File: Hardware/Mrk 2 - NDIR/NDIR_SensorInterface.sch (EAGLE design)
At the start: 6 parts, among them J1 CONN_I2C_SENSOR_BOARD_MOUNT_T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, J2 CONN_42.54, Q1 DMG3404

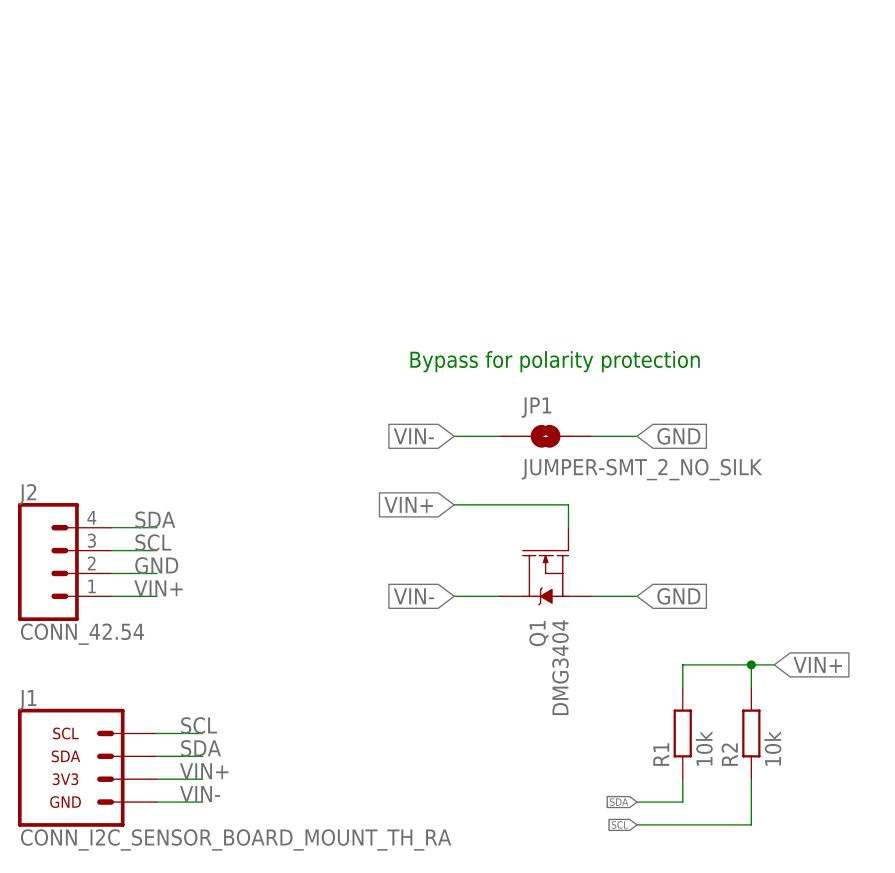
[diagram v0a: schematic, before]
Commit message: Fixed production version naming of Mrk 2 design
Added layout dimensions
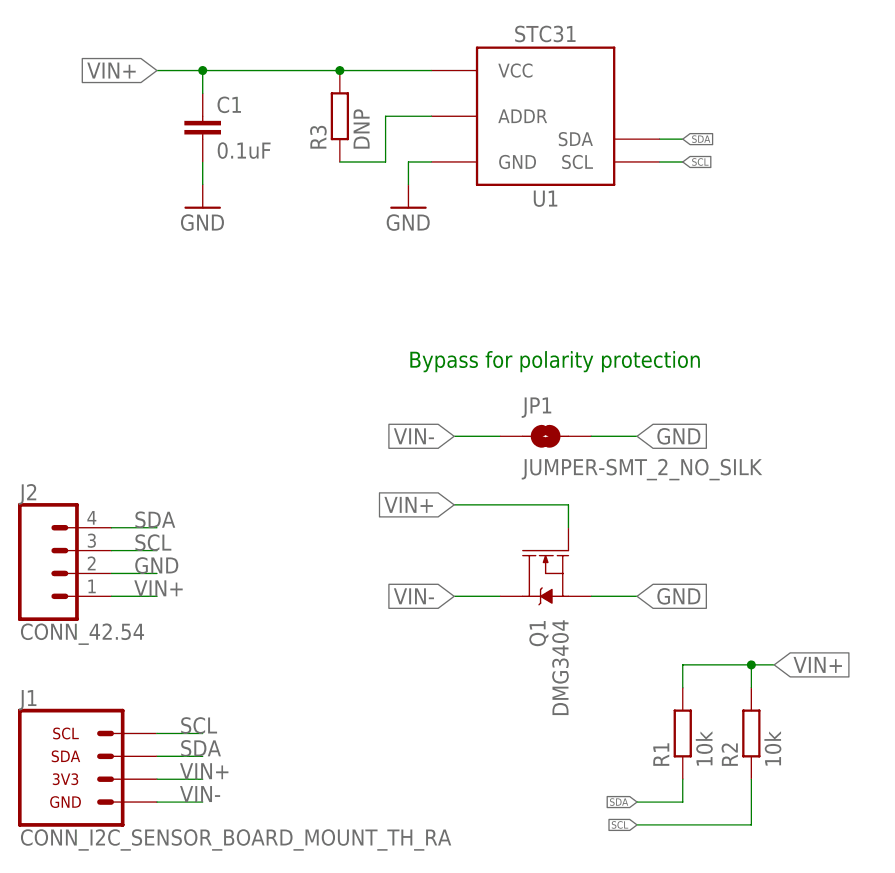
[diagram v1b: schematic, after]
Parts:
- added C1: 0.1uF, bschulz_passives:C-EU0.1UFC0603
- added R3: DNP, bschulz_passives:R-EU_R0603
- added U1: STC31, bschulz:STC31
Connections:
- new net N$2: R3.1, U1.ADDR
- net GND: now also C1.2, U1.GND
- net SCL: now also U1.SCL
- net SDA: now also U1.SDA
- net VIN+: now also C1.1, R3.2, U1.VCC
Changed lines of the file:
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@@
 <layer number="56" name="wert" color="7" fill="1" visible="no" active="no"/>
 <layer number="57" name="tCAD" color="7" fill="1" visible="no" active="no"/>
+<layer number="58" name="bCAD" color="7" fill="1" visible="no" active="no"/>
 <layer number="59" name="tCarbon" color="7" fill="1" visible="no" active="no"/>
 <layer number="60" name="bCarbon" color="7" fill="1" visible="no" active="no"/>
@@
 <layer number="128" name="_bValues" color="7" fill="1" visible="no" active="yes"/>
 <layer number="129" name="Mask" color="7" fill="1" visible="no" active="yes"/>
+<layer number="130" name="SMDSTROOK" color="7" fill="1" visible="no" active="no"/>
 <layer number="131" name="tAdjust" color="7" fill="1" visible="no" active="yes"/>
 <layer number="132" name="bAdjust" color="7" fill="1" visible="no" active="yes"/>
+<layer number="133" name="bottom_silk" color="7" fill="1" visible="no" active="no"/>
+<layer number="134" name="mbFinish" color="7" fill="1" visible="no" active="no"/>
+<layer number="135" name="mtGlue" color="7" fill="1" visible="no" active="no"/>
+<layer number="136" name="mbGlue" color="7" fill="1" visible="no" active="no"/>
+<layer number="137" name="mtTest" color="7" fill="1" visible="no" active="no"/>
+<layer number="138" name="mbTest" color="7" fill="1" visible="no" active="no"/>
+<layer number="139" name="mtKeepout" color="7" fill="1" visible="no" active="no"/>
+<layer number="140" name="mbKeepout" color="7" fill="1" visible="no" active="no"/>
+<layer number="141" name="mtRestrict" color="7" fill="1" visible="no" active="no"/>
+<layer number="142" name="mbRestrict" color="7" fill="1" visible="no" active="no"/>
+<layer number="143" name="mvRestrict" color="7" fill="1" visible="no" active="no"/>
 <layer number="144" name="Drill_legend" color="7" fill="1" visible="no" active="yes"/>
+<layer number="145" name="mHoles" color="7" fill="1" visible="no" active="no"/>
+<layer number="146" name="mMilling" color="7" fill="1" visible="no" active="no"/>
+<layer number="147" name="mMeasures" color="7" fill="1" visible="no" active="no"/>
+<layer number="148" name="mDocument" color="7" fill="1" visible="no" active="no"/>
+<layer number="149" name="mReference" color="7" fill="1" visible="no" active="no"/>
 <layer number="150" name="Notes" color="7" fill="1" visible="no" active="yes"/>
 <layer number="151" name="HeatSink" color="7" fill="1" visible="no" active="yes"/>
@@
 <layer number="154" name="FabDoc2" color="7" fill="1" visible="no" active="yes"/>
 <layer number="155" name="FabDoc3" color="7" fill="1" visible="no" active="yes"/>
+<layer number="166" name="AntennaArea" color="7" fill="1" visible="no" active="no"/>
+<layer number="168" name="4mmHeightArea" color="7" fill="1" visible="no" active="no"/>
+<layer number="191" name="mNets" color="7" fill="1" visible="no" active="no"/>
+<layer number="192" name="mBusses" color="7" fill="1" visible="no" active="no"/>
+<layer number="193" name="mPins" color="7" fill="1" visible="no" active="no"/>
+<layer number="194" name="mSymbols" color="7" fill="1" visible="no" active="no"/>
+<layer number="195" name="mNames" color="7" fill="1" visible="no" active="no"/>
+<layer number="196" name="mValues" color="7" fill="1" visible="no" active="no"/>
 <layer number="199" name="Contour" color="7" fill="1" visible="no" active="yes"/>
 <layer number="200" name="200bmp" color="7" fill="1" visible="no" active="yes"/>
@@
 <part name="R1" library="bschulz_passives" deviceset="R-EU_" device="R0603" technology="10K" value="10k"/>
 <part name="R2" library="bschulz_passives" deviceset="R-EU_" device="R0603" technology="10K" value="10k"/>
+<part name="U1" library="bschulz" deviceset="STC31" device=""/>
+<part name="R3" library="bschulz_passives" deviceset="R-EU_" device="R0603" value="DNP"/>
+<part name="C1" library="bschulz_passives" deviceset="C-EU" device="C0603" technology="0.1UF" value="0.1uF"/>
+<part name="GND1" library="supply1" library_urn="urn:adsk.eagle:library:371" deviceset="GND" device=""/>
+<part name="GND2" library="supply1" library_urn="urn:adsk.eagle:library:371" deviceset="GND" device=""/>
 </parts>
 <sheets>
@@
 <attribute name="VALUE" x="102.362" y="36.83" size="1.778" layer="96" rot="R90"/>
 </instance>
+<instance part="U1" gate="G$1" x="76.2" y="109.22" smashed="yes">
+<attribute name="DISP" x="76.2" y="118.364" size="1.778" layer="95" ratio="15" align="center"/>
+<attribute name="NAME" x="76.2" y="100.076" size="1.778" layer="95" ratio="15" align="center"/>
+</instance>
+<instance part="R3" gate="G$1" x="53.34" y="109.22" smashed="yes" rot="R90">
+<attribute name="NAME" x="51.8414" y="105.41" size="1.778" layer="95" rot="R90"/>
+<attribute name="VALUE" x="56.642" y="105.41" size="1.778" layer="96" rot="R90"/>
+</instance>
+<instance part="C1" gate="G$1" x="38.1" y="109.22" smashed="yes">
+<attribute name="NAME" x="39.624" y="109.601" size="1.778" layer="95"/>
+<attribute name="VALUE" x="39.624" y="104.521" size="1.778" layer="96"/>
+</instance>
+<instance part="GND1" gate="1" x="38.1" y="99.06" smashed="yes">
+<attribute name="VALUE" x="35.56" y="96.52" size="1.778" layer="96"/>
+</instance>
+<instance part="GND2" gate="1" x="60.96" y="99.06" smashed="yes">
+<attribute name="VALUE" x="58.42" y="96.52" size="1.778" layer="96"/>
+</instance>
 </instances>
 <busses>
@@
 <label x="86.36" y="73.66" size="1.778" layer="95" xref="yes"/>
 </segment>
+<segment>
+<pinref part="C1" gate="G$1" pin="2"/>
+<wire x1="38.1" y1="104.14" x2="38.1" y2="101.6" width="0.1524" layer="91"/>
+<pinref part="GND1" gate="1" pin="GND"/>
+</segment>
+<segment>
+<pinref part="U1" gate="G$1" pin="GND"/>
+<wire x1="63.5" y1="104.14" x2="60.96" y2="104.14" width="0.1524" layer="91"/>
+<wire x1="60.96" y1="104.14" x2="60.96" y2="101.6" width="0.1524" layer="91"/>
+<pinref part="GND2" gate="1" pin="GND"/>
+</segment>
 </net>
 <net name="SCL" class="0">
@@
 <label x="86.36" y="30.48" size="0.8128" layer="95" rot="R180" xref="yes"/>
 </segment>
+<segment>
+<pinref part="U1" gate="G$1" pin="SCL"/>
+<wire x1="88.9" y1="104.14" x2="91.44" y2="104.14" width="0.1524" layer="91"/>
+<label x="91.44" y="104.14" size="0.8128" layer="95" xref="yes"/>
+</segment>
 </net>
 <net name="SDA" class="0">
@@
 <wire x1="91.44" y1="33.02" x2="86.36" y2="33.02" width="0.1524" layer="91"/>
 <label x="86.36" y="33.02" size="0.8128" layer="95" rot="R180" xref="yes"/>
+</segment>
+<segment>
+<pinref part="U1" gate="G$1" pin="SDA"/>
+<wire x1="88.9" y1="106.68" x2="91.44" y2="106.68" width="0.1524" layer="91"/>
+<label x="91.44" y="106.68" size="0.8128" layer="95" xref="yes"/>
 </segment>
 </net>
@@
 <label x="101.6" y="48.26" size="1.778" layer="95" xref="yes"/>
 </segment>
+<segment>
+<pinref part="R3" gate="G$1" pin="2"/>
+<pinref part="U1" gate="G$1" pin="VCC"/>
+<wire x1="53.34" y1="114.3" x2="63.5" y2="114.3" width="0.1524" layer="91"/>
+<wire x1="53.34" y1="114.3" x2="38.1" y2="114.3" width="0.1524" layer="91"/>
+<junction x="53.34" y="114.3"/>
+<pinref part="C1" gate="G$1" pin="1"/>
+<wire x1="38.1" y1="114.3" x2="38.1" y2="111.76" width="0.1524" layer="91"/>
+<wire x1="38.1" y1="114.3" x2="33.02" y2="114.3" width="0.1524" layer="91"/>
+<junction x="38.1" y="114.3"/>
+<label x="33.02" y="114.3" size="1.778" layer="95" rot="R180" xref="yes"/>
+</segment>
+</net>
+<net name="N$2" class="0">
+<segment>
+<pinref part="R3" gate="G$1" pin="1"/>
+<wire x1="53.34" y1="104.14" x2="58.42" y2="104.14" width="0.1524" layer="91"/>
+<wire x1="58.42" y1="104.14" x2="58.42" y2="109.22" width="0.1524" layer="91"/>
+<pinref part="U1" gate="G$1" pin="ADDR"/>
+<wire x1="58.42" y1="109.22" x2="63.5" y2="109.22" width="0.1524" layer="91"/>
+</segment>
 </net>
 </nets>
@@
 </drawing>
 <compatibility>
+<note version="8.2" severity="warning">
+Since Version 8.2, EAGLE supports online libraries. The ids
+of those online libraries will not be understood (or retained)
+with this version.
+</note>
 <note version="8.3" severity="warning">
 Since Version 8.3, EAGLE supports URNs for individual library
